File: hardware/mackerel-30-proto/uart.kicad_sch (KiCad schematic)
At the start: 0 parts

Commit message: Add power and DUART
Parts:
- added C21, C22: 0.1uF, Capacitor_SMD:C_1210_3225Metric_Pad1.33x2.70mm_HandSolder, symbol Device:C
- added R1, R2: R, Resistor_THT:R_Axial_DIN0207_L6.3mm_D2.5mm_P7.62mm_Horizontal, symbol Device:R
- added U5: XR68C681, Package_LCC:PLCC-44_THT-Socket, symbol mackerel-68k-symbols:XR68C681
- added X1: 3.6864MHz, Oscillator:Oscillator_DIP-8, symbol Oscillator:CXO_DIP8
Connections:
- new net: R2.1, U5.24 (INTR)
- new net: U5.36 (X1/CLK), X1.5 (OUT)
- new net: R1.1, U5.41 (/IACK)
- new net +5V: C21.1, C22.1, R1.2, R2.2, U5.44 (VCC), X1.8 (Vcc)
- new net A1: U5.2 (A1)
- new net A2: U5.4 (A2)
- new net A3: U5.6 (A3)
- new net A4: U5.7 (A4)
- new net D24: U5.28 (D0)
- new net D25: U5.18 (D1)
- new net D26: U5.27 (D2)
- new net D27: U5.19 (D3)
- new net D28: U5.26 (D4)
- new net D29: U5.20 (D5)
- new net D30: U5.25 (D6)
- new net D31: U5.21 (D7)
- new net GND: C21.2, C22.2, U5.22 (GND), X1.4 (GND)
- new net RXA: U5.35 (RXDA)
- new net RXB: U5.11 (RXDB)
- new net R/W: U5.9 (/RW)
- new net TXA: U5.33 (TXDA)
- new net TXB: U5.13 (TXDB)
- no-connect marks 0 -> 2

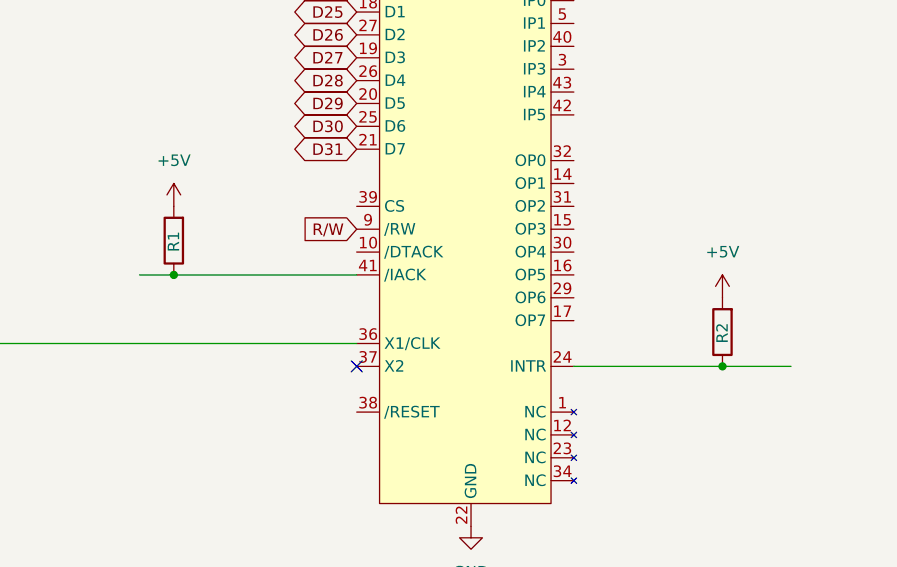
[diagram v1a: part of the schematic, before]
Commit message: Add 68882 FPU symbol
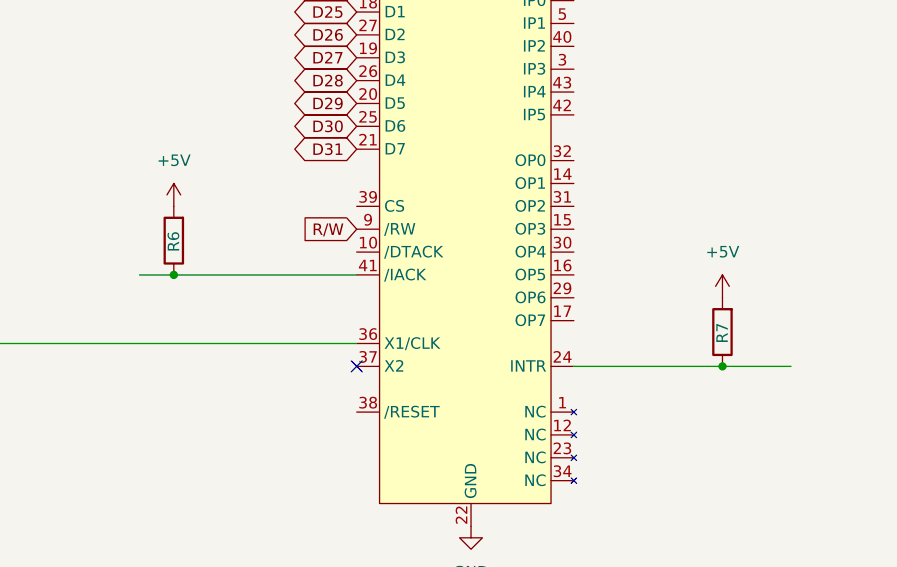
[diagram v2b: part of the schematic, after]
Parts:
- renumbered R1 to R6, R2 to R7
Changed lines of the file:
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@@
 		(dnp no)
 		(fields_autoplaced yes)
-		(property "Reference" "#PWR021"
+		(property "Reference" "#PWR024"
 			(at 232.41 39.37 0)
 			(effects
@@
 			(project "mackerel-30-proto"
 				(path "/9307474f-ec99-494d-b4c9-fbd0b10ce86a/d143ddc0-b4a1-490e-ae52-7a0ad9150902"
-					(reference "#PWR021")
+					(reference "#PWR024")
 					(unit 1)
 				)
@@
 		(on_board yes)
 		(dnp no)
-		(property "Reference" "R1"
+		(property "Reference" "R6"
 			(at 106.68 107.95 90)
 			(effects
@@
 			(project "mackerel-30-proto"
 				(path "/9307474f-ec99-494d-b4c9-fbd0b10ce86a/d143ddc0-b4a1-490e-ae52-7a0ad9150902"
-					(reference "R1")
+					(reference "R6")
 					(unit 1)
 				)
@@
 		(on_board yes)
 		(dnp no)
-		(property "Reference" "#PWR015"
+		(property "Reference" "#PWR018"
 			(at 73.66 114.3 0)
 			(effects
@@
 			(project "mackerel-30-proto"
 				(path "/9307474f-ec99-494d-b4c9-fbd0b10ce86a/d143ddc0-b4a1-490e-ae52-7a0ad9150902"
-					(reference "#PWR015")
+					(reference "#PWR018")
 					(unit 1)
 				)
@@
 		(on_board yes)
 		(dnp no)
-		(property "Reference" "#PWR016"
+		(property "Reference" "#PWR019"
 			(at 73.66 132.08 0)
 			(effects
@@
 			(project "mackerel-30-proto"
 				(path "/9307474f-ec99-494d-b4c9-fbd0b10ce86a/d143ddc0-b4a1-490e-ae52-7a0ad9150902"
-					(reference "#PWR016")
+					(reference "#PWR019")
 					(unit 1)
 				)
@@
 		(on_board yes)
 		(dnp no)
-		(property "Reference" "R2"
+		(property "Reference" "R7"
 			(at 167.64 118.11 90)
 			(effects
@@
 			(project "mackerel-30-proto"
 				(path "/9307474f-ec99-494d-b4c9-fbd0b10ce86a/d143ddc0-b4a1-490e-ae52-7a0ad9150902"
-					(reference "R2")
+					(reference "R7")
 					(unit 1)
 				)
@@
 		(dnp no)
 		(fields_autoplaced yes)
-		(property "Reference" "#PWR019"
+		(property "Reference" "#PWR022"
 			(at 139.7 144.78 0)
 			(effects
@@
 			(project "mackerel-30-proto"
 				(path "/9307474f-ec99-494d-b4c9-fbd0b10ce86a/d143ddc0-b4a1-490e-ae52-7a0ad9150902"
-					(reference "#PWR019")
+					(reference "#PWR022")
 					(unit 1)
 				)
@@
 		(dnp no)
 		(fields_autoplaced yes)
-		(property "Reference" "#PWR017"
+		(property "Reference" "#PWR020"
 			(at 106.68 106.68 0)
 			(effects
@@
 			(project "mackerel-30-proto"
 				(path "/9307474f-ec99-494d-b4c9-fbd0b10ce86a/d143ddc0-b4a1-490e-ae52-7a0ad9150902"
-					(reference "#PWR017")
+					(reference "#PWR020")
 					(unit 1)
 				)
@@
 		(dnp no)
 		(fields_autoplaced yes)
-		(property "Reference" "#PWR022"
+		(property "Reference" "#PWR025"
 			(at 240.03 52.07 0)
 			(effects
@@
 			(project "mackerel-30-proto"
 				(path "/9307474f-ec99-494d-b4c9-fbd0b10ce86a/d143ddc0-b4a1-490e-ae52-7a0ad9150902"
-					(reference "#PWR022")
+					(reference "#PWR025")
 					(unit 1)
 				)
@@
 		(dnp no)
 		(fields_autoplaced yes)
-		(property "Reference" "#PWR020"
+		(property "Reference" "#PWR023"
 			(at 167.64 116.84 0)
 			(effects
@@
 			(project "mackerel-30-proto"
 				(path "/9307474f-ec99-494d-b4c9-fbd0b10ce86a/d143ddc0-b4a1-490e-ae52-7a0ad9150902"
-					(reference "#PWR020")
+					(reference "#PWR023")
 					(unit 1)
 				)
@@
 		(on_board yes)
 		(dnp no)
-		(property "Reference" "#PWR018"
+		(property "Reference" "#PWR021"
 			(at 139.7 63.5 0)
 			(effects
@@
 			(project "mackerel-30-proto"
 				(path "/9307474f-ec99-494d-b4c9-fbd0b10ce86a/d143ddc0-b4a1-490e-ae52-7a0ad9150902"
-					(reference "#PWR018")
-					(unit 1)
-				)
+					(reference "#PWR021")
+					(unit 1)
+				)

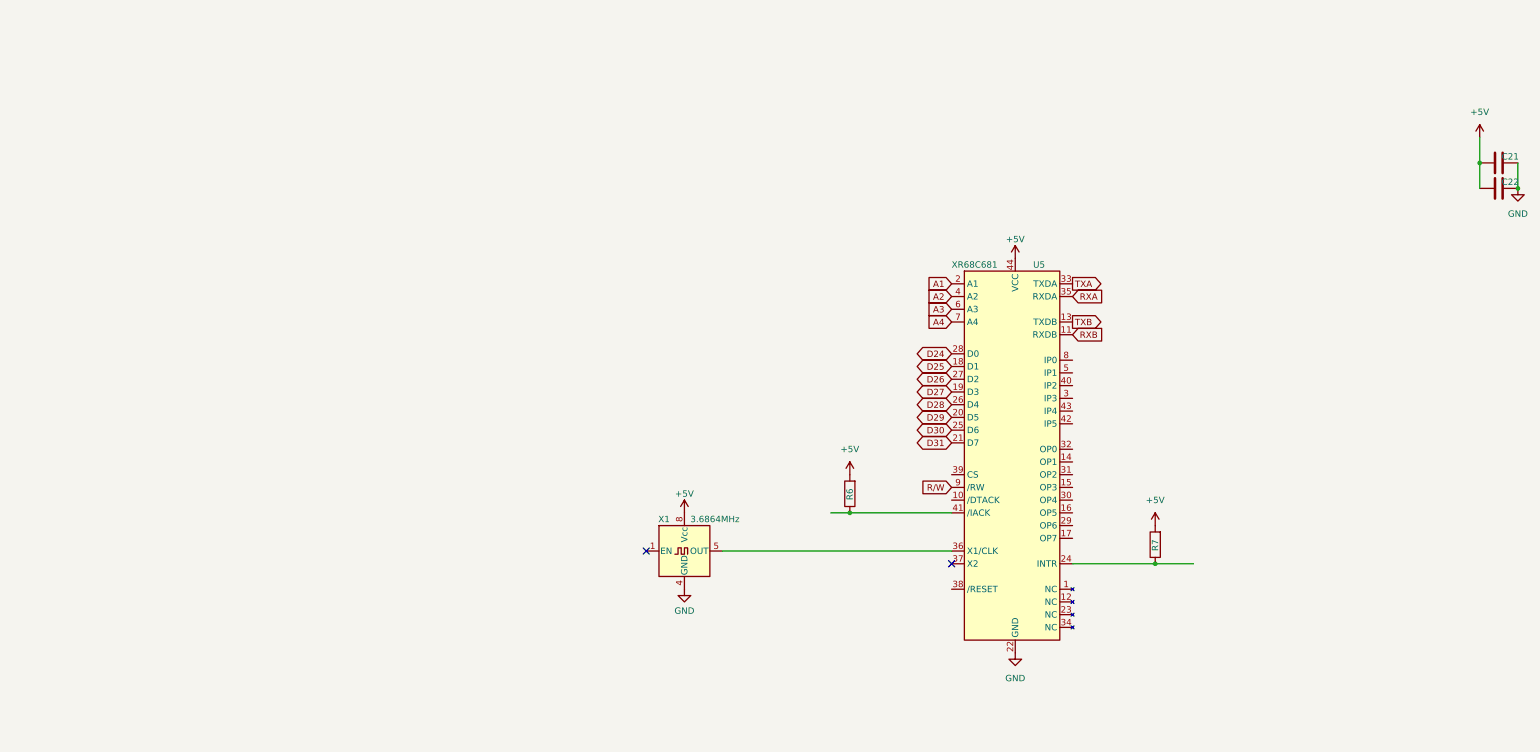
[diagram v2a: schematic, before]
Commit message: Wired most of the control signals for the CPU and DRAM
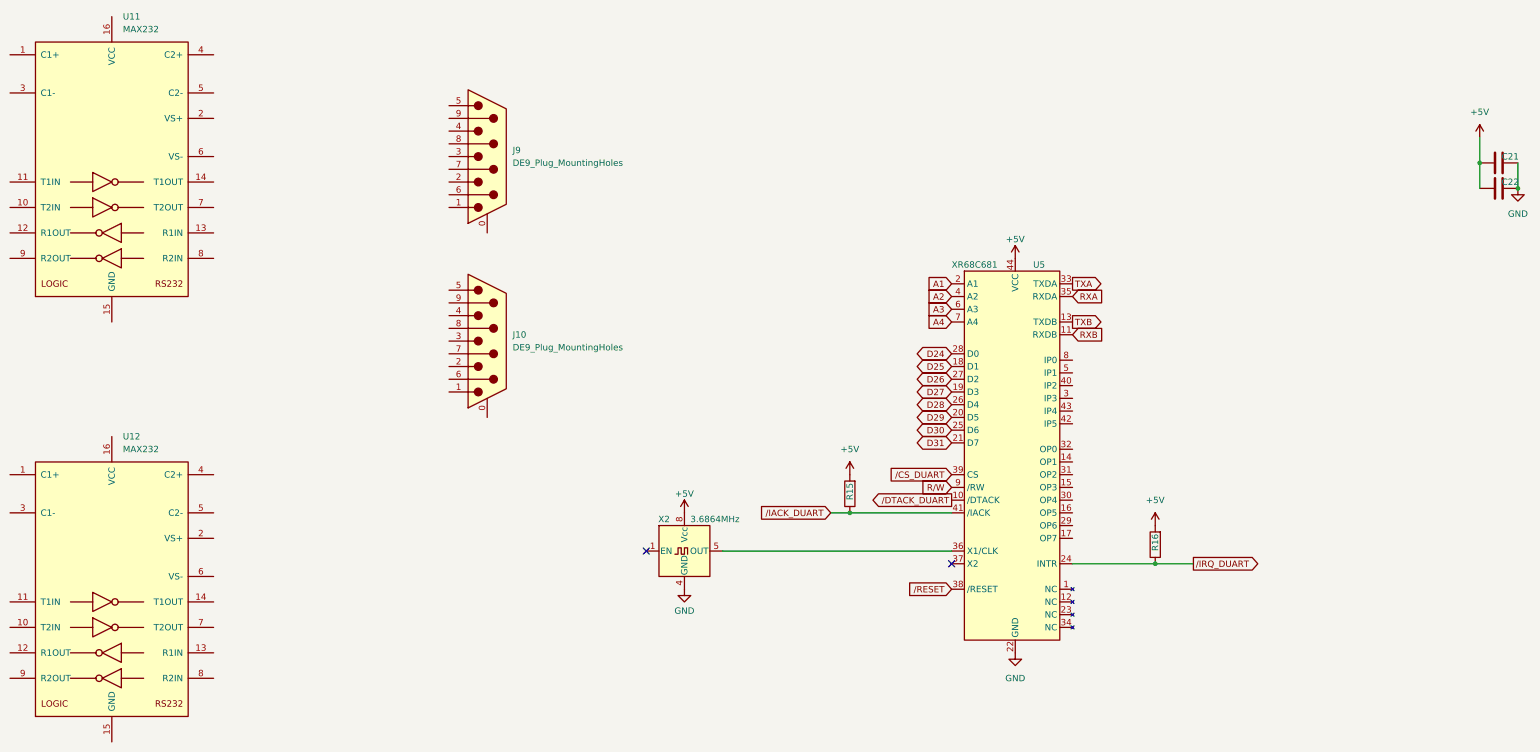
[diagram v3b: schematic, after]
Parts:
- added J10, J9: DE9_Plug_MountingHoles, Connector_Dsub:DSUB-9_Male_Horizontal_P2.77x2.84mm_EdgePinOffset7.70mm_Housed_MountingHolesOffset9.12mm, symbol Connector:DE9_Plug_MountingHoles
- added U11, U12: MAX232, Package_DIP:DIP-16_W7.62mm_Socket, symbol Interface_UART:MAX232
- renumbered R6 to R15, R7 to R16, X1 to X2
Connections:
- net /DTACK_DUART: now reaches U5.10 (/DTACK)
- net /IRQ_DUART: now reaches R16.1, U5.24 (INTR)
- net /RESET: now reaches U5.38 (/RESET)
- net /CS_DUART: now reaches U5.39 (CS)
- net /IACK_DUART: now reaches R15.1, U5.41 (/IACK)

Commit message: A bit of cleanup
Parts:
- removed J10, J9: DE9_Plug_MountingHoles, Connector_Dsub:DSUB-9_Male_Horizontal_P2.77x2.84mm_EdgePinOffset7.70mm_Housed_MountingHolesOffset9.12mm, symbol Connector:DE9_Plug_MountingHoles
- removed U11, U12: MAX232, Package_DIP:DIP-16_W7.62mm_Socket, symbol Interface_UART:MAX232
- renumbered R15 to R16, R16 to R17

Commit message: positioning
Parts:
- added J4, J5: Conn_01x06, Connector_PinHeader_2.54mm:PinHeader_1x06_P2.54mm_Vertical, symbol Connector_Generic:Conn_01x06
- added J6: Conn_02x10_Odd_Even, Connector_PinHeader_2.54mm:PinHeader_2x10_P2.54mm_Vertical, symbol Connector_Generic:Conn_02x10_Odd_Even
- C21, C22: footprint Capacitor_SMD:C_1210_3225Metric_Pad1.33x2.70mm_HandSolder -> Capacitor_SMD:C_1206_3216Metric_Pad1.33x1.80mm_HandSolder
- R16, R17: footprint Resistor_THT:R_Axial_DIN0207_L6.3mm_D2.5mm_P7.62mm_Horizontal -> Resistor_SMD:R_0805_2012Metric_Pad1.20x1.40mm_HandSolder
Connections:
- net +5V: now also J6.3 (Pin_3), J6.4 (Pin_4)
- net GND: now also J4.1 (Pin_1), J5.1 (Pin_1), J6.19 (Pin_19), J6.20 (Pin_20), J6.5 (Pin_5), J6.6 (Pin_6)
- net RXA: now also J4.4 (Pin_4)
- net RXB: now also J5.4 (Pin_4)
- net TXA: now also J4.5 (Pin_5)
- net TXB: now also J5.5 (Pin_5)
- net /RTSB: now reaches U5.14 (OP1)
- net /RTSB: now also J5.2 (Pin_2)
- net OP3: now reaches U5.15 (OP3)
- net OP3: now also J6.10 (Pin_10)
- net OP5: now reaches U5.16 (OP5)
- net OP5: now also J6.14 (Pin_14)
- net OP7: now reaches U5.17 (OP7)
- net OP7: now also J6.18 (Pin_18)
- net OP6: now reaches U5.29 (OP6)
- net OP6: now also J6.16 (Pin_16)
- net IP3: now reaches U5.3 (IP3)
- net IP3: now also J6.13 (Pin_13)
- net OP4: now reaches U5.30 (OP4)
- net OP4: now also J6.12 (Pin_12)
- net OP2: now reaches U5.31 (OP2)
- net OP2: now also J6.8 (Pin_8)
- net /RTSA: now reaches U5.32 (OP0)
- net /RTSA: now also J4.2 (Pin_2)
- net IP2: now reaches U5.40 (IP2)
- net IP2: now also J6.11 (Pin_11)
- net IP5: now reaches U5.42 (IP5)
- net IP5: now also J6.17 (Pin_17)
- net IP4: now reaches U5.43 (IP4)
- net IP4: now also J6.15 (Pin_15)
- net IP1: now reaches U5.5 (IP1)
- net IP1: now also J6.9 (Pin_9)
- net IP0: now reaches U5.8 (IP0)
- net IP0: now also J6.7 (Pin_7)
- new net +3.3V: J6.1 (Pin_1), J6.2 (Pin_2)
- no-connect marks 2 -> 6

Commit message: rough layout of the PCB components
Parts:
- C21, C22: footprint Capacitor_SMD:C_1206_3216Metric_Pad1.33x1.80mm_HandSolder -> Capacitor_THT:C_Disc_D4.3mm_W1.9mm_P5.00mm
- R15: renamed from R16; footprint Resistor_SMD:R_0805_2012Metric_Pad1.20x1.40mm_HandSolder -> Resistor_THT:R_Axial_DIN0207_L6.3mm_D2.5mm_P7.62mm_Horizontal
- R16: renamed from R17; footprint Resistor_SMD:R_0805_2012Metric_Pad1.20x1.40mm_HandSolder -> Resistor_THT:R_Axial_DIN0207_L6.3mm_D2.5mm_P7.62mm_Horizontal
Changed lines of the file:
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@@
 		(on_board yes)
 		(dnp no)
-		(property "Reference" "R16"
+		(property "Reference" "R15"
 			(at 106.68 107.95 90)
 			(effects
@@
 			)
 		)
-		(property "Footprint" "Resistor_SMD:R_0805_2012Metric_Pad1.20x1.40mm_HandSolder"
+		(property "Footprint" "Resistor_THT:R_Axial_DIN0207_L6.3mm_D2.5mm_P7.62mm_Horizontal"
 			(at 108.458 106.68 90)
 			(effects
@@
 			(project "mackerel-30-proto"
 				(path "/9307474f-ec99-494d-b4c9-fbd0b10ce86a/d143ddc0-b4a1-490e-ae52-7a0ad9150902"
-					(reference "R16")
+					(reference "R15")
 					(unit 1)
 				)
@@
 		(on_board yes)
 		(dnp no)
-		(property "Reference" "R17"
+		(property "Reference" "R16"
 			(at 167.64 118.11 90)
 			(effects
@@
 			)
 		)
-		(property "Footprint" "Resistor_SMD:R_0805_2012Metric_Pad1.20x1.40mm_HandSolder"
+		(property "Footprint" "Resistor_THT:R_Axial_DIN0207_L6.3mm_D2.5mm_P7.62mm_Horizontal"
 			(at 169.418 116.84 90)
 			(effects
@@
 			(project "mackerel-30-proto"
 				(path "/9307474f-ec99-494d-b4c9-fbd0b10ce86a/d143ddc0-b4a1-490e-ae52-7a0ad9150902"
-					(reference "R17")
+					(reference "R16")
 					(unit 1)
 				)
@@
 			)
 		)
-		(property "Footprint" "Capacitor_SMD:C_1206_3216Metric_Pad1.33x1.80mm_HandSolder"
+		(property "Footprint" "Capacitor_THT:C_Disc_D4.3mm_W1.9mm_P5.00mm"
 			(at 240.03 39.6748 0)
 			(effects
@@
 			)
 		)
-		(property "Footprint" "Capacitor_SMD:C_1206_3216Metric_Pad1.33x1.80mm_HandSolder"
+		(property "Footprint" "Capacitor_THT:C_Disc_D4.3mm_W1.9mm_P5.00mm"
 			(at 240.03 44.7548 0)
 			(effects
